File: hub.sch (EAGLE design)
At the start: 50 parts, among them IC1 SN65220DBV, IC2 SN65220DBV, IC3 SN65220DBV, IC4 SN65220DBV, IC5 SN65220DBV, U1 LM3526-L, X1 12MHz

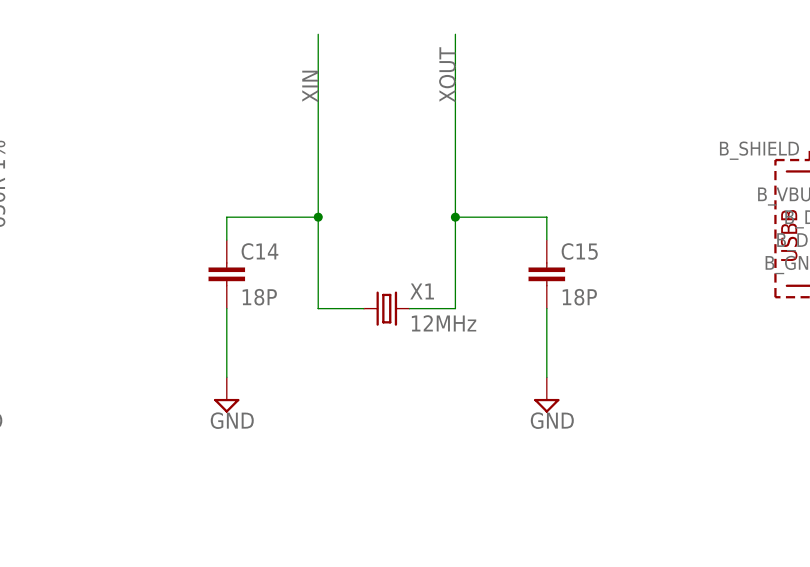
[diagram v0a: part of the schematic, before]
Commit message: switch to crystal with correct drive level (supporting 600μW)
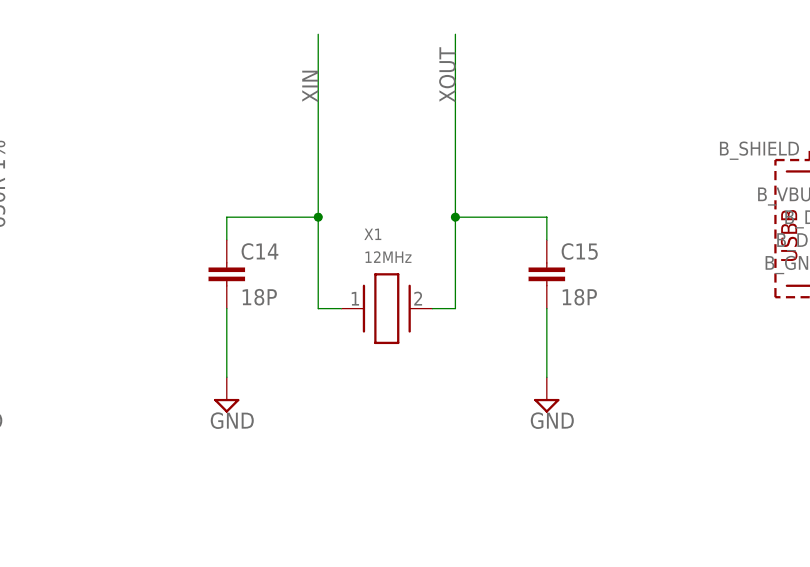
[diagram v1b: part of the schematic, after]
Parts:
- EC3, EC4, EC5, EC6: MPN (none) -> EEF-CD0D121R; OC_MOUSER (none) -> 667-EEF-CD0D121R
- U$1: MPN (none) -> CY7C65634-48AXCT; OC_MOUSER (none) -> 727-CY7C65634-48AXCT
- X1: device Ava:ABRACON_ABM3_CRYSTAL -> ABLS-12.000MHZ-B2-T:ABLS-12.000MHZ-B2-T; DIGIKEY (none) -> 535-9067-1-ND; MOUSER# 815-ABM3-12-D2Y-T -> (none); MPN (none) -> ABLS-12.000MHZ-B2-T; OC_MOUSER (none) -> 815-ABLS-12-B2

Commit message: pick 18pF caps
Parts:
- C14, C15: DIGIKEY (none) -> 1276-1089-1-ND; OC_MOUSER (none) -> 77-VJ0603A180JXACBC
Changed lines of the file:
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@@
 <part name="R3" library="rcl" library_urn="urn:adsk.eagle:library:334" deviceset="R-US_" device="M0805" package3d_urn="urn:adsk.eagle:package:23556/1" value="650R 1%"/>
 <part name="SUPPLY4" library="supply2" library_urn="urn:adsk.eagle:library:372" deviceset="GND" device=""/>
-<part name="C14" library="rcl" library_urn="urn:adsk.eagle:library:334" deviceset="C-EU" device="C0603" package3d_urn="urn:adsk.eagle:package:23616/2" value="18P"/>
-<part name="C15" library="rcl" library_urn="urn:adsk.eagle:library:334" deviceset="C-EU" device="C0603" package3d_urn="urn:adsk.eagle:package:23616/2" value="18P"/>
+<part name="C14" library="rcl" library_urn="urn:adsk.eagle:library:334" deviceset="C-EU" device="C0603" package3d_urn="urn:adsk.eagle:package:23616/2" value="18P">
+<attribute name="DIGIKEY" value="1276-1089-1-ND"/>
+<attribute name="OC_MOUSER" value="77-VJ0603A180JXACBC"/>
+</part>
+<part name="C15" library="rcl" library_urn="urn:adsk.eagle:library:334" deviceset="C-EU" device="C0603" package3d_urn="urn:adsk.eagle:package:23616/2" value="18P">
+<attribute name="DIGIKEY" value="1276-1089-1-ND"/>
+<attribute name="OC_MOUSER" value="77-VJ0603A180JXACBC"/>
+</part>
 <part name="SUPPLY5" library="supply2" library_urn="urn:adsk.eagle:library:372" deviceset="GND" device=""/>
 <part name="SUPPLY6" library="supply2" library_urn="urn:adsk.eagle:library:372" deviceset="GND" device=""/>
@@
 <instance part="R3" gate="G$1" x="129.54" y="-45.72" rot="R90"/>
 <instance part="SUPPLY4" gate="GND" x="129.54" y="-68.58"/>
-<instance part="C14" gate="G$1" x="157.48" y="-53.34"/>
-<instance part="C15" gate="G$1" x="193.04" y="-53.34"/>
+<instance part="C14" gate="G$1" x="157.48" y="-53.34">
+<attribute name="DIGIKEY" x="157.48" y="-53.34" size="1.778" layer="96" display="off"/>
+<attribute name="OC_MOUSER" x="157.48" y="-53.34" size="1.778" layer="96" display="off"/>
+</instance>
+<instance part="C15" gate="G$1" x="193.04" y="-53.34">
+<attribute name="DIGIKEY" x="193.04" y="-53.34" size="1.778" layer="96" display="off"/>
+<attribute name="OC_MOUSER" x="193.04" y="-53.34" size="1.778" layer="96" display="off"/>
+</instance>
 <instance part="SUPPLY5" gate="GND" x="157.48" y="-68.58"/>
 <instance part="SUPPLY6" gate="GND" x="193.04" y="-68.58"/>

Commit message: Switch to 0805 capacitors for consistency
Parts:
- C14, C15: device rcl:C-EUC0603 -> rcl:C-EUC0805
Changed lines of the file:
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@@
 <part name="R3" library="rcl" library_urn="urn:adsk.eagle:library:334" deviceset="R-US_" device="M0805" package3d_urn="urn:adsk.eagle:package:23556/1" value="650R 1%"/>
 <part name="SUPPLY4" library="supply2" library_urn="urn:adsk.eagle:library:372" deviceset="GND" device=""/>
-<part name="C14" library="rcl" library_urn="urn:adsk.eagle:library:334" deviceset="C-EU" device="C0603" package3d_urn="urn:adsk.eagle:package:23616/2" value="18P">
+<part name="C14" library="rcl" library_urn="urn:adsk.eagle:library:334" deviceset="C-EU" device="C0805" package3d_urn="urn:adsk.eagle:package:23617/2" value="18P">
 <attribute name="DIGIKEY" value="1276-1089-1-ND"/>
 <attribute name="OC_MOUSER" value="77-VJ0603A180JXACBC"/>
 </part>
-<part name="C15" library="rcl" library_urn="urn:adsk.eagle:library:334" deviceset="C-EU" device="C0603" package3d_urn="urn:adsk.eagle:package:23616/2" value="18P">
+<part name="C15" library="rcl" library_urn="urn:adsk.eagle:library:334" deviceset="C-EU" device="C0805" package3d_urn="urn:adsk.eagle:package:23617/2" value="18P">
 <attribute name="DIGIKEY" value="1276-1089-1-ND"/>
 <attribute name="OC_MOUSER" value="77-VJ0603A180JXACBC"/>

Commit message: Switch EC3, EC4, EC5, EC6 to ELXY250ELL121MF15D from vendor BOM
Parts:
- EC1: DIGIKEY (none) -> PCE3878CT-ND; MPN (none) -> EEE-1CA100SR; OC_MOUSER (none) -> 667-EEE-1CA100SR
- EC2: DIGIKEY (none) -> 338-3973-1-ND; MPN (none) -> UUP1C4R7MCL1GS; OC_MOUSER (none) -> 647-UUP1C4R7MCL1GS
- EC3, EC4, EC5, EC6: device rcl:CPOL-USUD-5X5,8 -> SparkFun-Capacitors:100UF-POLAR-RADIAL-2.5MM-25V-20%; DIGIKEY (none) -> 565-1791-ND; MPN EEF-CD0D121R -> ELXY250ELL121MF15D; OC_MOUSER 667-EEF-CD0D121R -> 661-ELXY250ELL121MF1
- J1, J3: DIGIKEY (none) -> 732-2107-ND; MPN (none) -> 61400826021; OC_MOUSER (none) -> 710-61400826021
- U$1: DIGIKEY (none) -> 428-3153-1-ND
- U1: DIGIKEY (none) -> LM3526MX-L/NOPBCT-ND; MPN (none) -> LM3526MX-L/NOPB; OC_MOUSER (none) -> 926-LM3526MX-L/NOPB

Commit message: update EC1 with same footprint as EC3-EC6
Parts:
- EC1: device rcl:CPOL-USUD-5X5,8 -> SparkFun-Capacitors:100UF-POLAR-RADIAL-2.5MM-25V-20%; DIGIKEY PCE3878CT-ND -> 493-16013-1-ND; MF (none) -> nichicon; MPN EEE-1CA100SR -> UST1H100MDD1TE; OC_MOUSER 667-EEE-1CA100SR -> 647-UST1H100MDD1TE
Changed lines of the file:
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@@
 <part name="C1" library="rcl" library_urn="urn:adsk.eagle:library:334" deviceset="C-EU" device="C0805" package3d_urn="urn:adsk.eagle:package:23617/2" value="0.1uF"/>
 <part name="SUPPLY17" library="supply2" library_urn="urn:adsk.eagle:library:372" deviceset="GND" device=""/>
-<part name="EC1" library="rcl" library_urn="urn:adsk.eagle:library:334" deviceset="CPOL-US" device="UD-5X5,8" package3d_urn="urn:adsk.eagle:package:23470/1" value="10uF">
-<attribute name="DIGIKEY" value="PCE3878CT-ND"/>
-<attribute name="MPN" value="EEE-1CA100SR"/>
-<attribute name="OC_MOUSER" value="667-EEE-1CA100SR"/>
+<part name="EC1" library="SparkFun-Capacitors" library_urn="urn:adsk.eagle:library:510" deviceset="100UF-POLAR" device="-RADIAL-2.5MM-25V-20%" package3d_urn="urn:adsk.eagle:package:37415/1" value="10uF">
+<attribute name="DIGIKEY" value="493-16013-1-ND"/>
+<attribute name="MF" value="nichicon"/>
+<attribute name="MPN" value="UST1H100MDD1TE"/>
+<attribute name="OC_MOUSER" value="647-UST1H100MDD1TE"/>
 </part>
 <part name="C2" library="rcl" library_urn="urn:adsk.eagle:library:334" deviceset="C-EU" device="C0805" package3d_urn="urn:adsk.eagle:package:23617/2" value="1uF"/>
@@
 <attribute name="MPN" x="68.58" y="25.4" size="1.778" layer="96" display="off"/>
 <attribute name="OC_MOUSER" x="68.58" y="25.4" size="1.778" layer="96" display="off"/>
+<attribute name="MF" x="68.58" y="25.4" size="1.778" layer="96" display="off"/>
 </instance>
 <instance part="C2" gate="G$1" x="114.3" y="25.4"/>

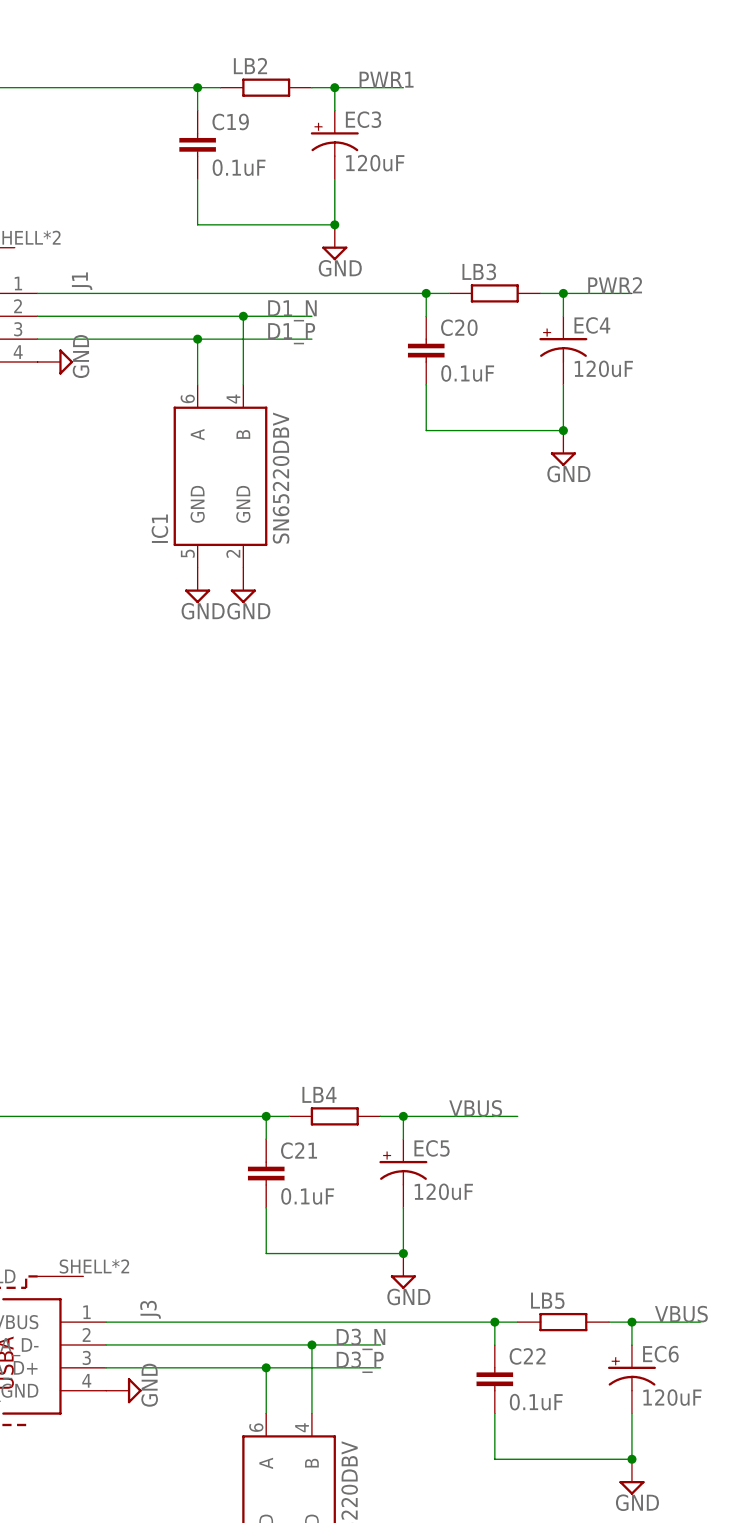
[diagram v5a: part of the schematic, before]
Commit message: pick ferrite beads
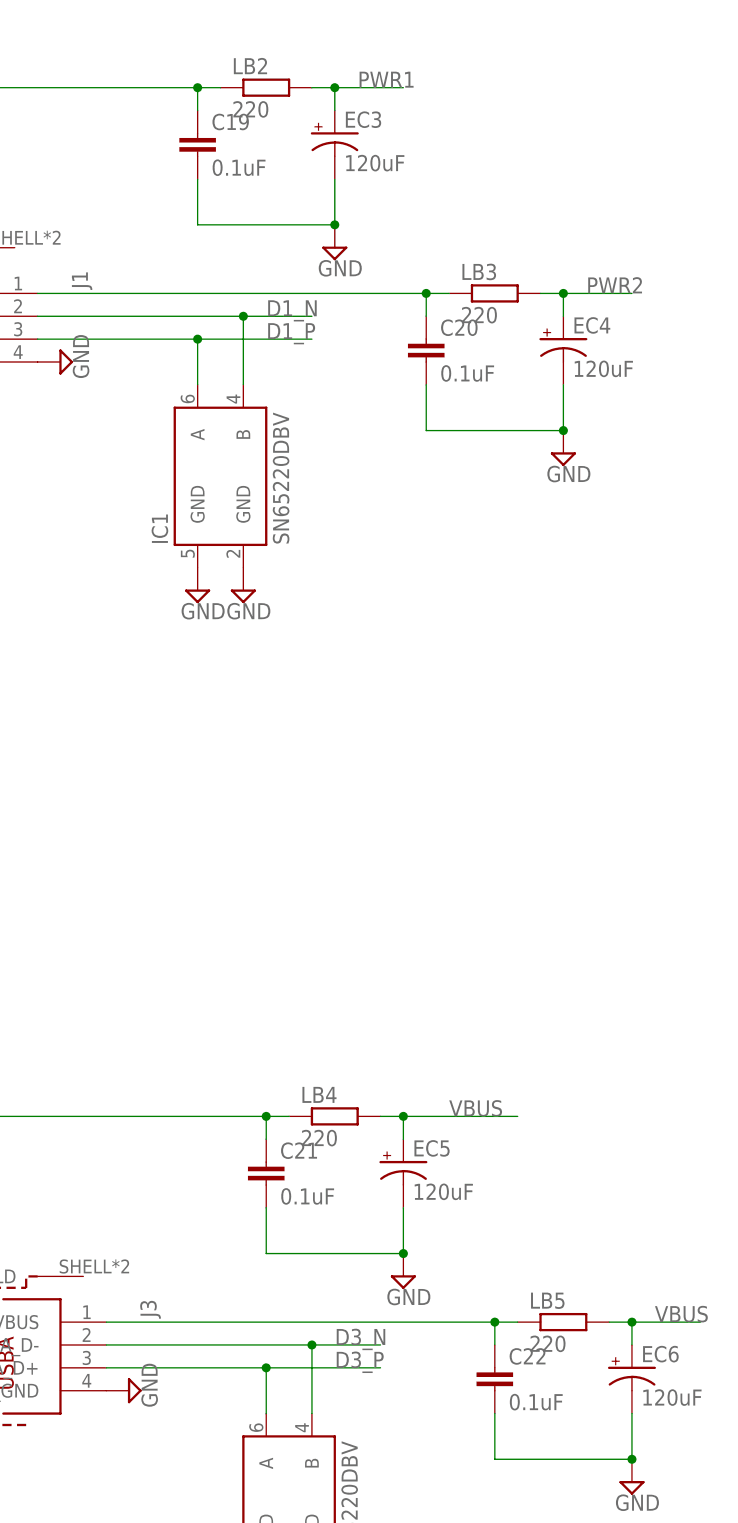
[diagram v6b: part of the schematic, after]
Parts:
- LB2, LB3, LB4, LB5: value (none) -> 220; DIGIKEY (none) -> 490-1054-1-ND; MPN (none) -> BLM21PG221SN1D; OC_MOUSER (none) -> 81-BLM21P221SG
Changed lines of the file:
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@@
 <attribute name="OC_MOUSER" value="661-ELXY250ELL121MF1"/>
 </part>
-<part name="LB2" library="rcl" library_urn="urn:adsk.eagle:library:334" deviceset="R-EU_" device="R0805" package3d_urn="urn:adsk.eagle:package:23553/2"/>
+<part name="LB2" library="rcl" library_urn="urn:adsk.eagle:library:334" deviceset="R-EU_" device="R0805" package3d_urn="urn:adsk.eagle:package:23553/2" value="220">
+<attribute name="DIGIKEY" value="490-1054-1-ND"/>
+<attribute name="MPN" value="BLM21PG221SN1D"/>
+<attribute name="OC_MOUSER" value="81-BLM21P221SG"/>
+</part>
 <part name="C16" library="rcl" library_urn="urn:adsk.eagle:library:334" deviceset="C-EU" device="C0805" package3d_urn="urn:adsk.eagle:package:23617/2" value="0.1uF"/>
 <part name="EC2" library="rcl" library_urn="urn:adsk.eagle:library:334" deviceset="CPOL-US" device="UD-5X5,8" package3d_urn="urn:adsk.eagle:package:23470/1" value="4.3uF">
@@
 <attribute name="OC_MOUSER" value="661-ELXY250ELL121MF1"/>
 </part>
-<part name="LB3" library="rcl" library_urn="urn:adsk.eagle:library:334" deviceset="R-EU_" device="R0805" package3d_urn="urn:adsk.eagle:package:23553/2"/>
+<part name="LB3" library="rcl" library_urn="urn:adsk.eagle:library:334" deviceset="R-EU_" device="R0805" package3d_urn="urn:adsk.eagle:package:23553/2" value="220">
+<attribute name="DIGIKEY" value="490-1054-1-ND"/>
+<attribute name="MPN" value="BLM21PG221SN1D"/>
+<attribute name="OC_MOUSER" value="81-BLM21P221SG"/>
+</part>
 <part name="IC2" library="sn65220_40" deviceset="SN65220" device="DBV"/>
 <part name="SUPPLY15" library="supply2" library_urn="urn:adsk.eagle:library:372" deviceset="GND" device=""/>
@@
 <attribute name="OC_MOUSER" value="661-ELXY250ELL121MF1"/>
 </part>
-<part name="LB4" library="rcl" library_urn="urn:adsk.eagle:library:334" deviceset="R-EU_" device="R0805" package3d_urn="urn:adsk.eagle:package:23553/2"/>
+<part name="LB4" library="rcl" library_urn="urn:adsk.eagle:library:334" deviceset="R-EU_" device="R0805" package3d_urn="urn:adsk.eagle:package:23553/2" value="220">
+<attribute name="DIGIKEY" value="490-1054-1-ND"/>
+<attribute name="MPN" value="BLM21PG221SN1D"/>
+<attribute name="OC_MOUSER" value="81-BLM21P221SG"/>
+</part>
 <part name="IC4" library="sn65220_40" deviceset="SN65220" device="DBV"/>
 <part name="SUPPLY29" library="supply2" library_urn="urn:adsk.eagle:library:372" deviceset="GND" device=""/>
@@
 <attribute name="OC_MOUSER" value="661-ELXY250ELL121MF1"/>
 </part>
-<part name="LB5" library="rcl" library_urn="urn:adsk.eagle:library:334" deviceset="R-EU_" device="R0805" package3d_urn="urn:adsk.eagle:package:23553/2"/>
+<part name="LB5" library="rcl" library_urn="urn:adsk.eagle:library:334" deviceset="R-EU_" device="R0805" package3d_urn="urn:adsk.eagle:package:23553/2" value="220">
+<attribute name="DIGIKEY" value="490-1054-1-ND"/>
+<attribute name="MPN" value="BLM21PG221SN1D"/>
+<attribute name="OC_MOUSER" value="81-BLM21P221SG"/>
+</part>
 <part name="IC5" library="sn65220_40" deviceset="SN65220" device="DBV"/>
 <part name="SUPPLY33" library="supply2" library_urn="urn:adsk.eagle:library:372" deviceset="GND" device=""/>
@@
 <attribute name="OC_MOUSER" x="276.86" y="86.36" size="1.778" layer="96" display="off"/>
 </instance>
-<instance part="LB2" gate="G$1" x="269.24" y="91.44"/>
+<instance part="LB2" gate="G$1" x="269.24" y="91.44">
+<attribute name="DIGIKEY" x="269.24" y="91.44" size="1.778" layer="96" display="off"/>
+<attribute name="MPN" x="269.24" y="91.44" size="1.778" layer="96" display="off"/>
+<attribute name="OC_MOUSER" x="269.24" y="91.44" size="1.778" layer="96" display="off"/>
+</instance>
 <instance part="C16" gate="G$1" x="91.44" y="76.2"/>
 <instance part="EC2" gate="G$1" x="114.3" y="76.2">
@@
 <attribute name="OC_MOUSER" x="302.26" y="63.5" size="1.778" layer="96" display="off"/>
 </instance>
-<instance part="LB3" gate="G$1" x="294.64" y="68.58"/>
+<instance part="LB3" gate="G$1" x="294.64" y="68.58">
+<attribute name="DIGIKEY" x="294.64" y="68.58" size="1.778" layer="96" display="off"/>
+<attribute name="MPN" x="294.64" y="68.58" size="1.778" layer="96" display="off"/>
+<attribute name="OC_MOUSER" x="294.64" y="68.58" size="1.778" layer="96" display="off"/>
+</instance>
 <instance part="IC2" gate="G$1" x="226.06" y="25.4" rot="R90"/>
 <instance part="SUPPLY15" gate="GND" x="223.52" y="12.7"/>
@@
 <attribute name="OC_MOUSER" x="284.48" y="-27.94" size="1.778" layer="96" display="off"/>
 </instance>
-<instance part="LB4" gate="G$1" x="276.86" y="-22.86"/>
+<instance part="LB4" gate="G$1" x="276.86" y="-22.86">
+<attribute name="DIGIKEY" x="276.86" y="-22.86" size="1.778" layer="96" display="off"/>
+<attribute name="MPN" x="276.86" y="-22.86" size="1.778" layer="96" display="off"/>
+<attribute name="OC_MOUSER" x="276.86" y="-22.86" size="1.778" layer="96" display="off"/>
+</instance>
 <instance part="IC4" gate="G$1" x="271.78" y="-66.04" rot="R90"/>
 <instance part="SUPPLY29" gate="GND" x="274.32" y="-78.74"/>
@@
 <attribute name="OC_MOUSER" x="309.88" y="-50.8" size="1.778" layer="96" display="off"/>
 </instance>
-<instance part="LB5" gate="G$1" x="302.26" y="-45.72"/>
+<instance part="LB5" gate="G$1" x="302.26" y="-45.72">
+<attribute name="DIGIKEY" x="302.26" y="-45.72" size="1.778" layer="96" display="off"/>
+<attribute name="MPN" x="302.26" y="-45.72" size="1.778" layer="96" display="off"/>
+<attribute name="OC_MOUSER" x="302.26" y="-45.72" size="1.778" layer="96" display="off"/>
+</instance>
 <instance part="IC5" gate="G$1" x="233.68" y="-88.9" rot="R90"/>
 <instance part="SUPPLY33" gate="GND" x="231.14" y="-101.6"/>

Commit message: pick wire-to-board connector
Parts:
- J2: DIGIKEY (none) -> A100039-ND; MF (none) -> te; MPN (none) -> 440054-7; OC_MOUSER (none) -> 571-440054-7
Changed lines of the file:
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@@
 <attribute name="OC_MOUSER" value="710-61400826021"/>
 </part>
-<part name="J2" library="Wire-to-Board (rev17c)" deviceset="62000711622" device=""/>
+<part name="J2" library="Wire-to-Board (rev17c)" deviceset="62000711622" device="">
+<attribute name="DIGIKEY" value="A100039-ND"/>
+<attribute name="MF" value="te"/>
+<attribute name="MPN" value="440054-7"/>
+<attribute name="OC_MOUSER" value="571-440054-7"/>
+</part>
 <part name="U$1" library="CY7C65634-48AXCT" deviceset="CY7C65634-48AXCT" device="">
 <attribute name="DIGIKEY" value="428-3153-1-ND"/>
@@
 <attribute name="OC_MOUSER" x="228.6" y="66.04" size="1.778" layer="96" rot="R270" display="off"/>
 </instance>
-<instance part="J2" gate="G$1" x="48.26" y="88.9"/>
+<instance part="J2" gate="G$1" x="48.26" y="88.9">
+<attribute name="DIGIKEY" x="48.26" y="88.9" size="1.778" layer="96" display="off"/>
+<attribute name="MF" x="48.26" y="88.9" size="1.778" layer="96" display="off"/>
+<attribute name="MPN" x="48.26" y="88.9" size="1.778" layer="96" display="off"/>
+<attribute name="OC_MOUSER" x="48.26" y="88.9" size="1.778" layer="96" display="off"/>
+</instance>
 <instance part="U$1" gate="G$1" x="0" y="0">
 <attribute name="MPN" x="0" y="0" size="1.778" layer="96" display="off"/>
